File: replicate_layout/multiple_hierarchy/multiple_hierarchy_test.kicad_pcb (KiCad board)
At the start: 2 copper layers, 72 parts, among them J1001 Pusa_4mm, J1002 Pusa_4mm, J201 Pusa_4mm, J202 Pusa_4mm, J601 Pusa_4mm, J602 Pusa_4mm, Q1101 CSD19531KCS, Q1102 CSD19531KCS, Q1301 CSD19531KCS, Q1302 CSD19531KCS, Q1401 CSD19531KCS, Q1402 CSD19531KCS, Q301 CSD19531KCS, Q302 CSD19531KCS, Q501 CSD19531KCS, Q502 CSD19531KCS, Q701 CSD19531KCS, Q702 CSD19531KCS, Q901 CSD19531KCS, Q902 CSD19531KCS, U101 TMS320F28027DA, U1101 IR2181, U1201 INA240, U1301 IR2181, U1401 IR2181, U301 IR2181, U401 INA240, U501 IR2181, U701 IR2181, U801 INA240, U901 IR2181

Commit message: Updated test projects
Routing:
- net -VDC: track 121.4 -> 121.8 mm, vias 0 -> 8

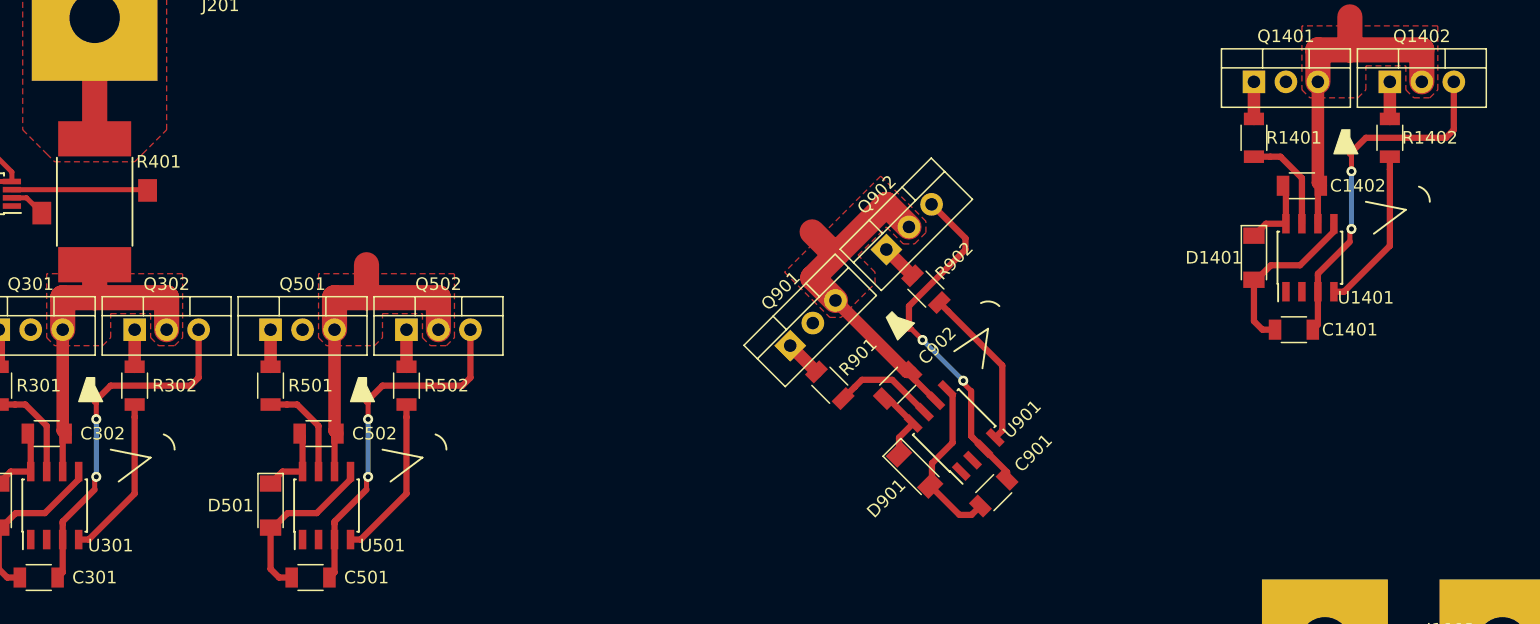
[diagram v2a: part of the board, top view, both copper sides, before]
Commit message: Modified test layouts so that one footprint is on bottom layer
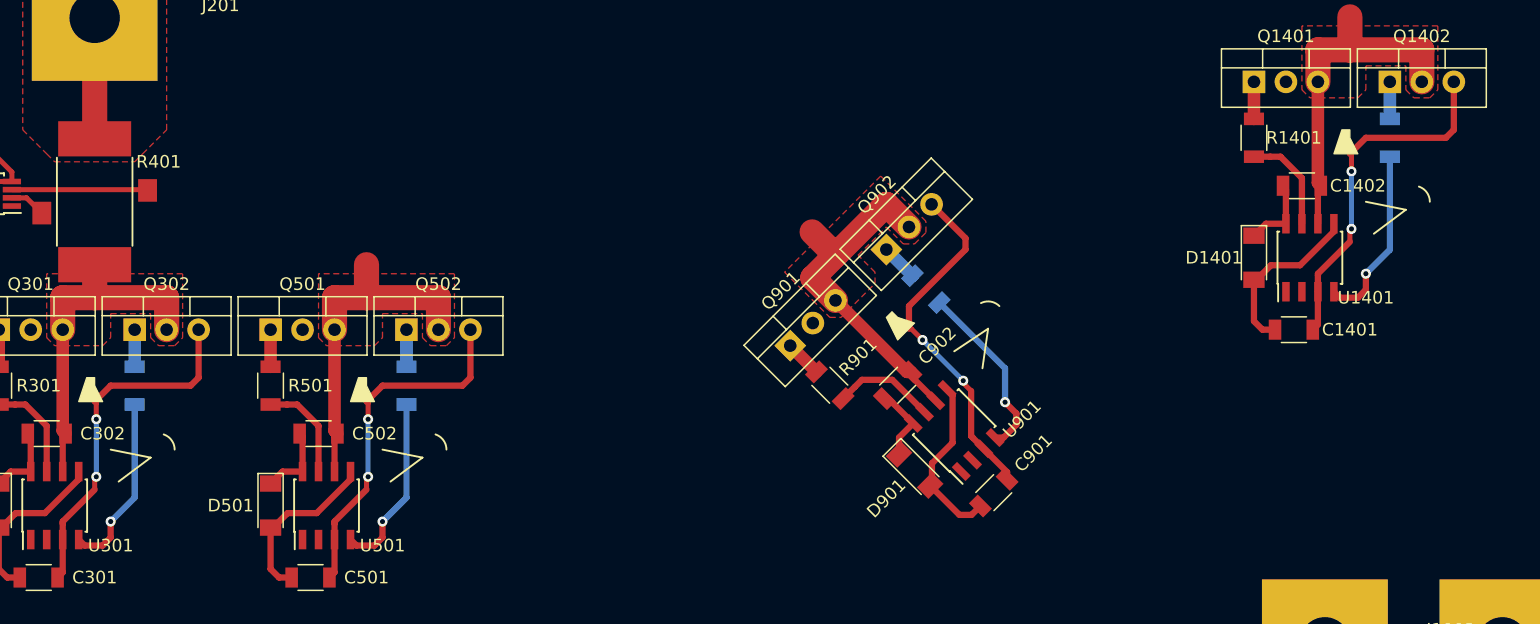
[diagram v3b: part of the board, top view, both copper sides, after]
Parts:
- R1402, R302, R502, R902: moved to B.Cu
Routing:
- net Net-(R1402-Pad1): track 13.0 -> 14.4 mm, vias 0 -> 1
- net Net-(R302-Pad1): track 13.0 -> 14.4 mm, vias 0 -> 1
- net Net-(R502-Pad1): track 13.0 -> 14.4 mm, vias 0 -> 1
- net Net-(R902-Pad1): track 13.0 -> 14.4 mm, vias 0 -> 1
